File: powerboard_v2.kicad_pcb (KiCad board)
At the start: 2 copper layers, 1 part

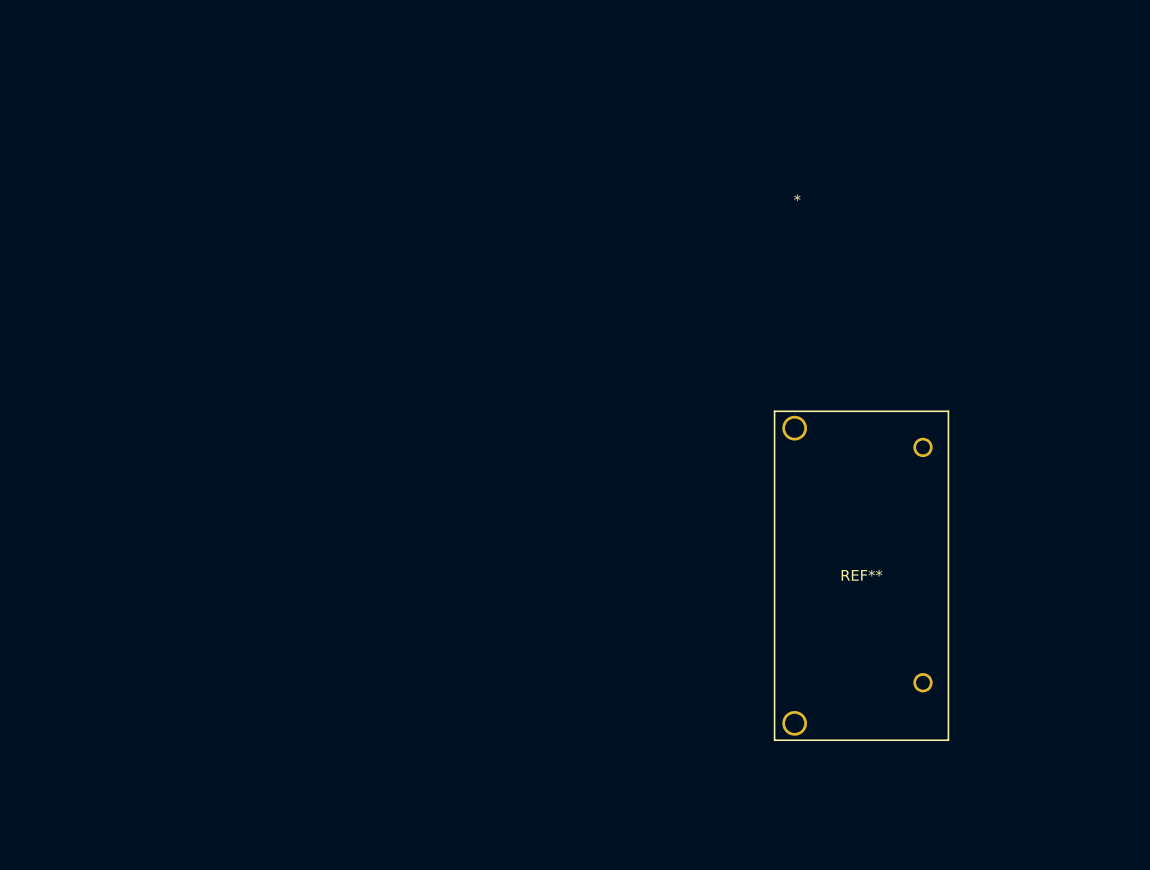
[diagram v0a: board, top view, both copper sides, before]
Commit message: 回路構成の変更、フットプリントの割り当て、部品配置
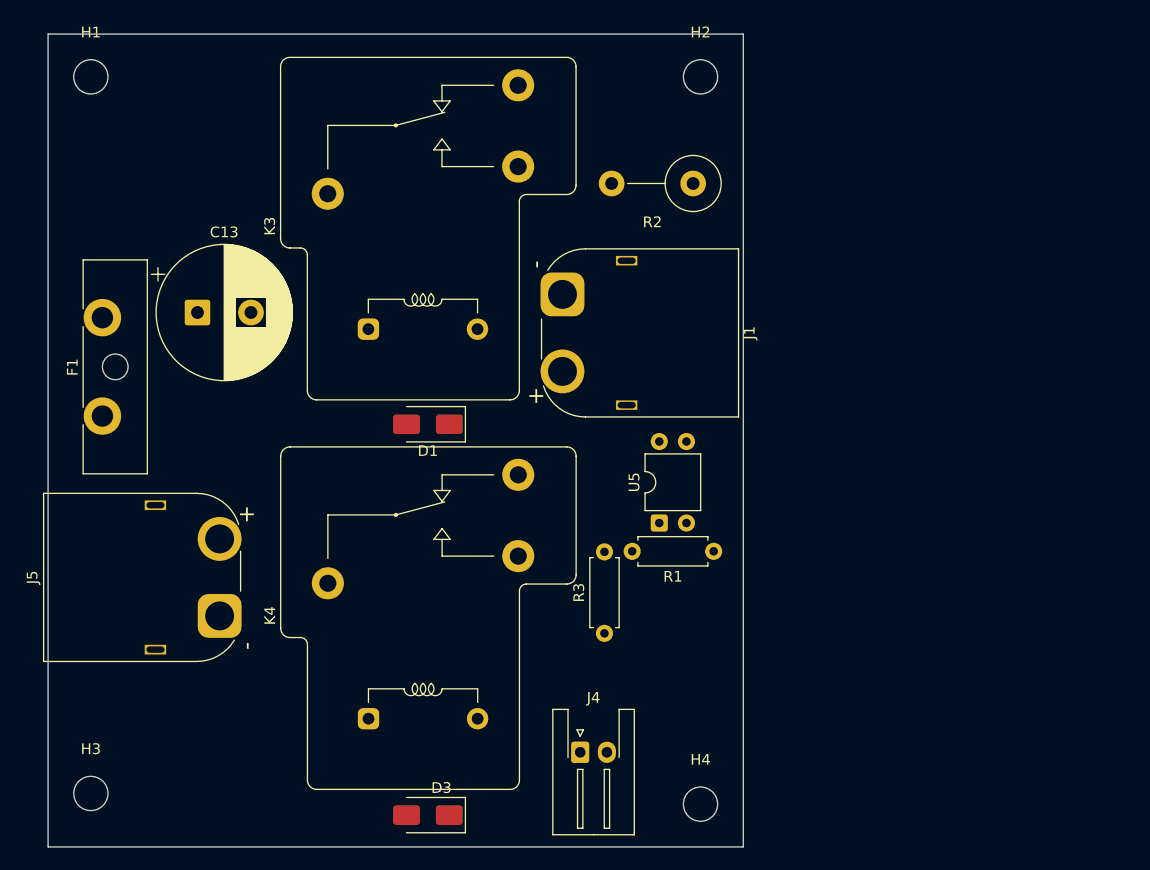
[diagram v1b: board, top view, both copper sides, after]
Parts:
- removed REF**: RELAY_G6QE-1A_OMR, footprints:RELAY_G6QE-1A_OMR
- added C13: C_Polarized 1000uf, Capacitor_THT:CP_Radial_D12.5mm_P5.00mm, F.Cu at (64.0, 76.0)
- added D1: D, Diode_SMD:D_SMA, F.Cu at (85.5, 86.5)
- added D3: D, Diode_SMD:D_SMA, F.Cu at (85.5, 123.0)
- added F1: Fuse, Fuse:Fuseholder_Blade_ATO_Littelfuse_Pudenz_2_Pin, F.Cu at (55.1, 85.7)
- added H1: MountingHole, MountingHole:MountingHole_3.2mm_M3, F.Cu at (54.0, 54.0)
- added H2: MountingHole, MountingHole:MountingHole_3.2mm_M3, F.Cu at (111.0, 54.0)
- added H3: MountingHole, MountingHole:MountingHole_3.2mm_M3, F.Cu at (54.0, 121.0)
- added H4: MountingHole, MountingHole:MountingHole_3.2mm_M3, F.Cu at (111.0, 122.0)
- added J1: Conn_01x02_Pin, Connector_AMASS:AMASS_XT60PW-M_1x02_P7.20mm_Horizontal, F.Cu at (98.1, 74.3)
- added J4: Conn_01x02_Pin, Connector_JST:JST_XH_S2B-XH-A-1_1x02_P2.50mm_Horizontal, F.Cu at (99.8, 117.2)
- added J5: Conn_01x02_Pin, Connector_AMASS:AMASS_XT60PW-M_1x02_P7.20mm_Horizontal, F.Cu at (66.0, 104.4)
- added K3: Relay_SPDT, Relay_THT:Relay_SPDT_RAYEX-L90S, F.Cu at (85.0, 80.1)
- added K4: Relay_SPDT, Relay_THT:Relay_SPDT_RAYEX-L90S, F.Cu at (85.1, 116.5)
- added R1: 1k, Resistor_THT:R_Axial_DIN0207_L6.3mm_D2.5mm_P7.62mm_Horizontal, F.Cu at (112.2, 98.4)
- added R2: 100, Resistor_THT:R_Axial_DIN0516_L15.5mm_D5.0mm_P7.62mm_Vertical, F.Cu at (110.3, 64.0)
- added R3: 70, Resistor_THT:R_Axial_DIN0207_L6.3mm_D2.5mm_P7.62mm_Horizontal, F.Cu at (102.0, 106.0)
- added U5: TLP785, Package_DIP:DIP-4_W7.62mm, F.Cu at (107.1, 95.7)
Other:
- board outline added: 65 x 76 mm

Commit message: 配線前最終版
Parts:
- removed F1: Fuse, Fuse:Fuseholder_Blade_ATO_Littelfuse_Pudenz_2_Pin
- moved J1 46.2 mm to (67.2, 108.6), turned to 90 degrees
- moved R1 39.6 mm to (150.2, 87.3)
- moved R3 39.6 mm to (140.0, 95.0)
- moved U5 39.6 mm to (145.1, 84.7)
- moved J4 39.6 mm to (137.7, 106.1)
- moved J5 32.7 mm to (98.7, 106.1), turned to -90 degrees
- moved C13 13.3 mm to (60.0, 88.7)
- moved R2 10.8 mm to (102.1, 71.0)
- moved D1 2.65 mm to (83.0, 85.6)
- moved K3 2.25 mm to (83.0, 79.2)
- moved D3 1.96 mm to (83.7, 122.4)
- moved K4 1.38 mm to (83.8, 116.0)
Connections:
- C13 pad 1: +24V -> xt60_out
- J1 pad 1: unconnected-(J1-Pin_1-Pad1) -> GND
- J5 pad 2: Net-(J5-Pin_2) -> +24V
- K3 pad 11: +24V -> xt60_out
- K3 pad 14: xt60_out -> +24V
- K3 pad A1: photo in -> +24V
- K3 pad A2: +24V -> photo in
- K4 pad 11: +24V -> xt60_out
- K4 pad 14: xt60_out -> +24V
- K4 pad A1: photo in -> +24V
- K4 pad A2: +24V -> photo in
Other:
- board size 65 x 76 mm -> 65 x 76.1 mm

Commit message: ver1かんせい
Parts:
- added G***: LOGO, LOGO, B.Cu at (76.2, 112.7)
- R2: footprint Resistor_THT:R_Axial_DIN0516_L15.5mm_D5.0mm_P7.62mm_Vertical -> Resistor_THT:R_Axial_DIN0516_L15.5mm_D5.0mm_P5.08mm_Vertical
- moved R1 93.6 mm to (58.3, 69.7), turned to 0 degrees
- moved J4 91.0 mm to (57.7, 62.7), turned to -90 degrees
- moved R3 82.5 mm to (65.9, 58.9), turned to -90 degrees
- moved U5 81.4 mm to (64.6, 72.9), turned to -90 degrees
- moved C13 3.71 mm to (62.7, 91.3), turned to 90 degrees
- moved R2 3.24 mm to (98.9, 70.3)
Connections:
- K3 pad A1: +24V -> photo in
- K3 pad A2: photo in -> +24V
- K4 pad A1: +24V -> photo in
- K4 pad A2: photo in -> +24V
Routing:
- net +24V: track 0.00 -> 140.2 mm, vias 0 -> 1
- net GND: track 0.00 -> 78.5 mm, vias 0 -> 64
- net photo in: track 0.00 -> 74.0 mm
- net cap out: track 0.00 -> 55.2 mm
- net xt60_out: track 0.00 -> 51.3 mm
- net GND1: track 0.00 -> 9.83 mm
- net +3.3V: track 0.00 -> 9.77 mm
- net Net-(R1-Pad2): track 0.00 -> 6.88 mm
- added copper zone on B.Cu, net GND
- added copper zone on F.Cu, net GND
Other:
- board size 65 x 76.1 mm -> 65 x 76 mm
- board text added: "+ -"
- board text added: "24v in"
- board text added: "A"

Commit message: 製造用出力
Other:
- board text added: "24V in"
- board text added: "24V out"
- board text added: "Signal in"
- board text removed: "24v in"
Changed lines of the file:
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@@
 		(tags "connector JST XH horizontal")
 		(property "Reference" "J4"
-			(at 1.25 -5.1 90)
+			(at 1.5548 -3.6618 270)
 			(layer "F.SilkS")
 			(effects
@@
 		(layer "Edge.Cuts")
 	)
+	(gr_text "24V out\n\n"
+		(at 57.2898 118.8086 0)
+		(layer "F.SilkS")
+		(effects
+			(font
+				(size 2 2)
+				(thickness 0.3)
+			)
+			(justify left bottom)
+		)
+	)
 	(gr_text "+       -"
 		(at 106.7182 121.374 90)
@@
 				(size 3 3)
 				(thickness 0.3)
-			)
-			(justify left bottom)
-		)
-	)
-	(gr_text "24v in"
-		(at 102.8066 100.3428 90)
-		(layer "F.SilkS")
-		(effects
-			(font
-				(size 1.5 1.5)
-				(thickness 0.3)
-				(bold yes)
 			)
 			(justify left bottom)
@@
 		)
 	)
+	(gr_text "24V in\n"
+		(at 95.7708 113.8302 90)
+		(layer "F.SilkS")
+		(effects
+			(font
+				(size 2 2)
+				(thickness 0.3)
+			)
+			(justify left bottom)
+		)
+	)
+	(gr_text "Signal in"
+		(at 62.827 60.87 270)
+		(layer "F.SilkS")
+		(effects
+			(font
+				(size 1 1)
+				(thickness 0.1)
+			)
+			(justify left bottom)
+		)
+	)
 	(gr_text "+       -"
 		(at 54.4704 93.0276 270)
@@
 	)
 	(gr_text_box "有明高専ロボット研究部\n電源基板2026ver1\nby T.ichimaru\n"
-		(start 57.2898 114.5414)
-		(end 72.86 123.0758)
+		(start 57.1882 116.5734)
+		(end 72.7584 123.2028)
 		(margins 1.0025 1.0025 1.0025 1.0025)
 		(layer "F.SilkS")

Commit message: ver2粗方完成(粗はある)
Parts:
- removed D3: D, Diode_SMD:D_SMA
- removed K4: Relay_SPDT, Relay_THT:Relay_SPDT_RAYEX-L90S
- added C1: 220uf, Capacitor_THT:CP_Radial_D10.0mm_P5.00mm, F.Cu at (69.9, 58.3)
- added C10: 2200pf, Capacitor_SMD:C_0603_1608Metric_Pad1.08x0.95mm_HandSolder, F.Cu at (85.6, 66.8)
- added C2: 4.7uf, Capacitor_SMD:C_0603_1608Metric_Pad1.08x0.95mm_HandSolder, F.Cu at (76.7, 59.8)
- added C3: 4.7uf, Capacitor_SMD:C_0603_1608Metric_Pad1.08x0.95mm_HandSolder, F.Cu at (76.7, 58.3)
- added C4: 0.1uf, Capacitor_SMD:C_0603_1608Metric_Pad1.08x0.95mm_HandSolder, F.Cu at (73.8, 65.3)
- added C5: 1uf, Capacitor_SMD:C_0603_1608Metric_Pad1.08x0.95mm_HandSolder, F.Cu at (76.2, 70.7)
- added C6: 2200pf, Capacitor_SMD:C_0603_1608Metric_Pad1.08x0.95mm_HandSolder, F.Cu at (68.7, 72.0)
- added C7: 22uf, Resistor_SMD:R_0603_1608Metric_Pad0.98x0.95mm_HandSolder, F.Cu at (102.2, 70.9)
- added C8: 22uf, Resistor_SMD:R_0603_1608Metric_Pad0.98x0.95mm_HandSolder, F.Cu at (103.7, 70.9)
- added C9: 22uf, Resistor_SMD:R_0603_1608Metric_Pad0.98x0.95mm_HandSolder, F.Cu at (105.2, 70.9)
- added J2: Conn_01x02_Pin, Connector_AMASS:AMASS_XT30PW-F_1x02_P2.50mm_Horizontal, F.Cu at (64.2, 70.5)
- added J3: Conn_01x02_Pin, Connector_AMASS:AMASS_XT30PW-F_1x02_P2.50mm_Horizontal, F.Cu at (108.2, 63.0)
- added JP1: SolderJumper_2_Open, Jumper:SolderJumper-2_P1.3mm_Open_RoundedPad1.0x1.5mm, F.Cu at (56.8, 80.3)
- added JP2: SolderJumper_2_Open, Jumper:SolderJumper-2_P1.3mm_Open_RoundedPad1.0x1.5mm, F.Cu at (66.3, 77.3)
- added L1: 22uH, Inductor_THT:L_Radial_D12.0mm_P5.00mm_Neosid_SD12k_style2, F.Cu at (92.7, 68.3)
- added R4: 20k, Resistor_SMD:R_0603_1608Metric_Pad0.98x0.95mm_HandSolder, F.Cu at (72.0, 72.0)
- added R5: 164k, Resistor_SMD:R_0603_1608Metric_Pad0.98x0.95mm_HandSolder, F.Cu at (68.7, 70.0)
- added R6: 0, Resistor_SMD:R_0603_1608Metric_Pad0.98x0.95mm_HandSolder, F.Cu at (86.5, 69.7)
- added U2: BD99010EFV-ME2, BD99010:HTSSOP-B24_ROM, F.Cu at (80.1, 65.0)
- moved J4 60.2 mm to (115.8, 78.7), turned to 90 degrees
- moved R1 56.4 mm to (113.0, 83.1), turned to -90 degrees
- moved R3 55.7 mm to (116.0, 83.1)
- moved U5 49.0 mm to (110.4, 90.3), turned to 180 degrees
- moved K3 28.6 mm to (86.9, 107.5)
- moved D1 28.4 mm to (86.4, 113.7)
- moved G*** 22.1 mm to (85.0, 133.0)
- moved R2 13.1 mm to (105.0, 81.9), turned to 90 degrees
- moved J5 10.1 mm to (103.8, 97.4)
- moved H4 7.81 mm to (116.0, 116.0)
- moved H2 5.00 mm to (116.0, 54.0)
- moved H3 5.00 mm to (54.0, 116.0)
- moved C13 3.82 mm to (66.4, 90.3)
- moved J1 2.09 mm to (66.5, 106.6)
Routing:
- net +24V: track 140.2 -> 42.1 mm, vias 1 -> 0
- net +7.5V: track 0.00 -> 78.2 mm, vias 0 -> 1
- net GND: track 78.5 -> 13.2 mm, vias 64 -> 0
- net cap out: track 55.2 -> 11.5 mm
- net photo in: track 74.0 -> 37.7 mm
- net GND2: track 0.00 -> 24.0 mm, vias 0 -> 90
- net +3V3: track 0.00 -> 21.6 mm
- net xt60_out: track 51.3 -> 30.9 mm
- net Net-(L1-Pad1): track 0.00 -> 15.5 mm
- net Net-(U2-RT): track 0.00 -> 8.33 mm
- net Net-(U2-COMP): track 0.00 -> 7.20 mm
- net +3.3V: track 9.77 -> 4.04 mm
- net Net-(U2-FPWM): track 0.00 -> 5.52 mm
- net GND1: track 9.83 -> 13.7 mm
- net Net-(U2-REG_L): track 0.00 -> 1.92 mm
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- added copper zone on B.Cu, net GND2
- added copper zone on F.Cu, net GND2
- added copper zone on F.Cu, net Net-(L1-Pad1)
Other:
- board size 65 x 76 mm -> 70 x 70 mm
- board text removed: "+ -"
- board text removed: "24V in"
- board text removed: "24V out"
- board text removed: "A"
- board text removed: "Signal in"
